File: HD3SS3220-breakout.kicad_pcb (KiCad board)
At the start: 4 copper layers, 74.1 x 58 mm, 30 parts, among them J2 USB_C_Receptacle, SW2 SW_DIP_x04, U4 HD3SS3220RNHR, U5 U-A-39SS-Y-1, U6 HT7533-1_C14289, U7 TPD4EUSB30, U8 TPD2EUSB30, U9 PZ254-2-08-WS

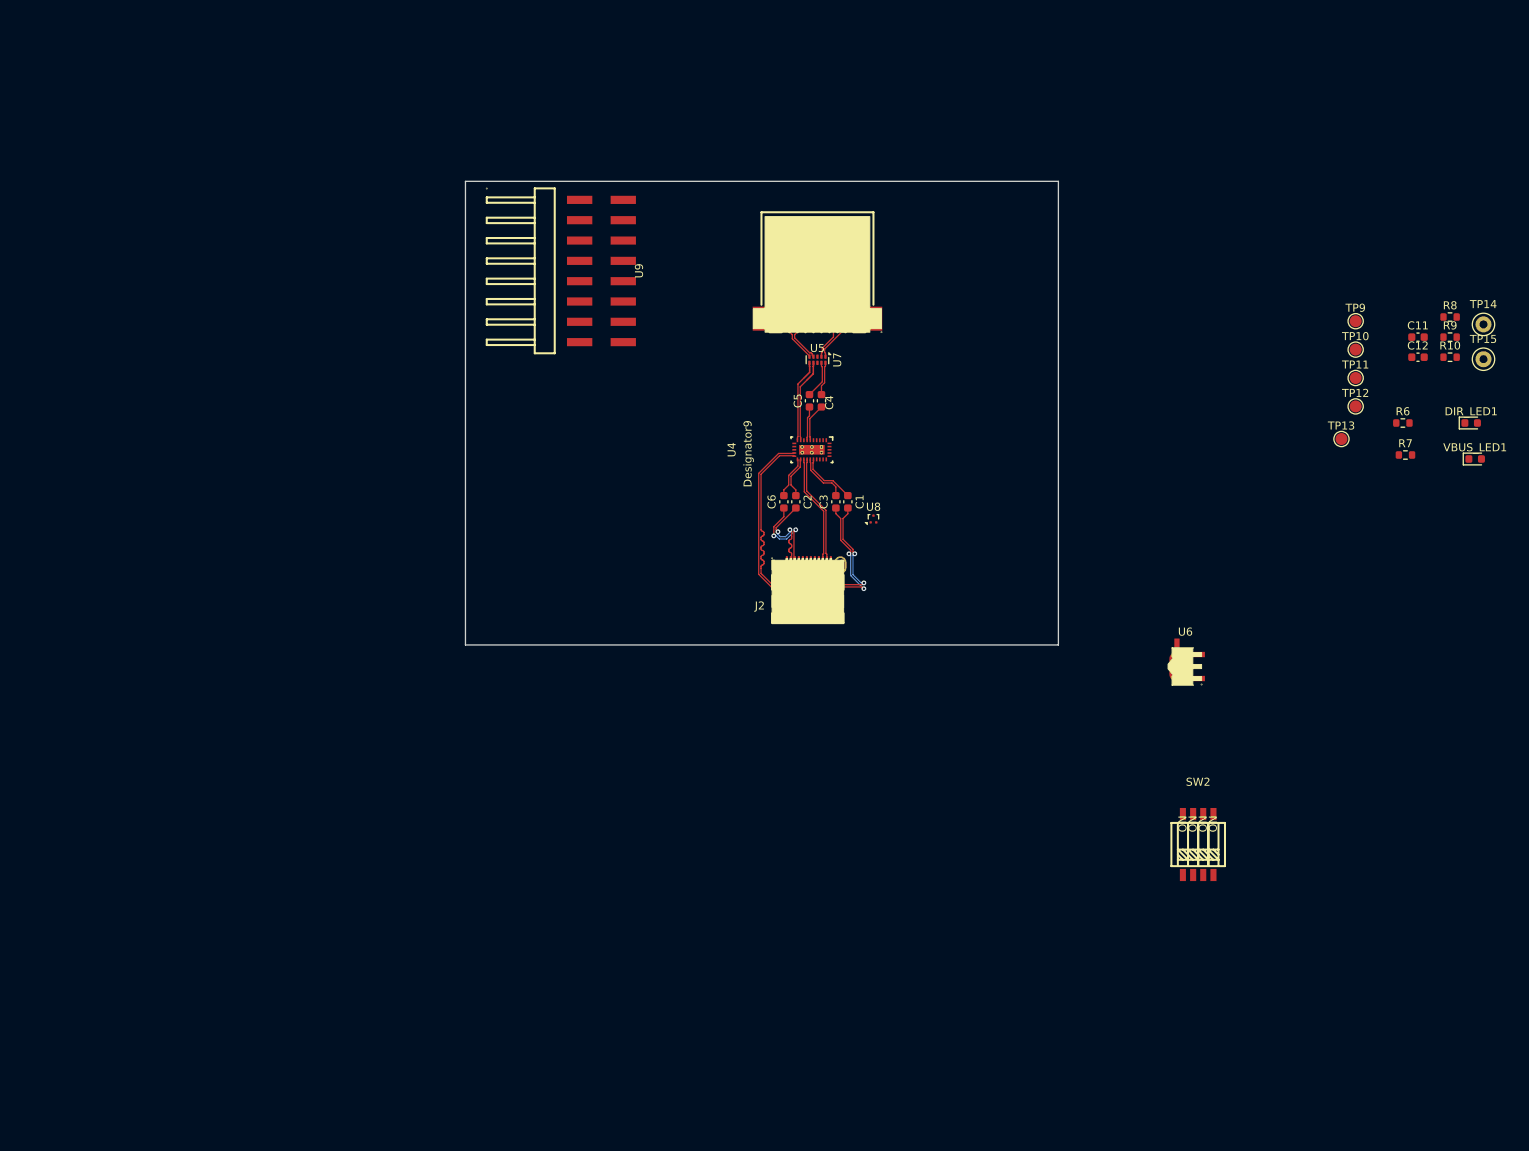
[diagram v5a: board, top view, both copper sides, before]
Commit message: Routing Complete (DRC Checker Errors needs fixing)
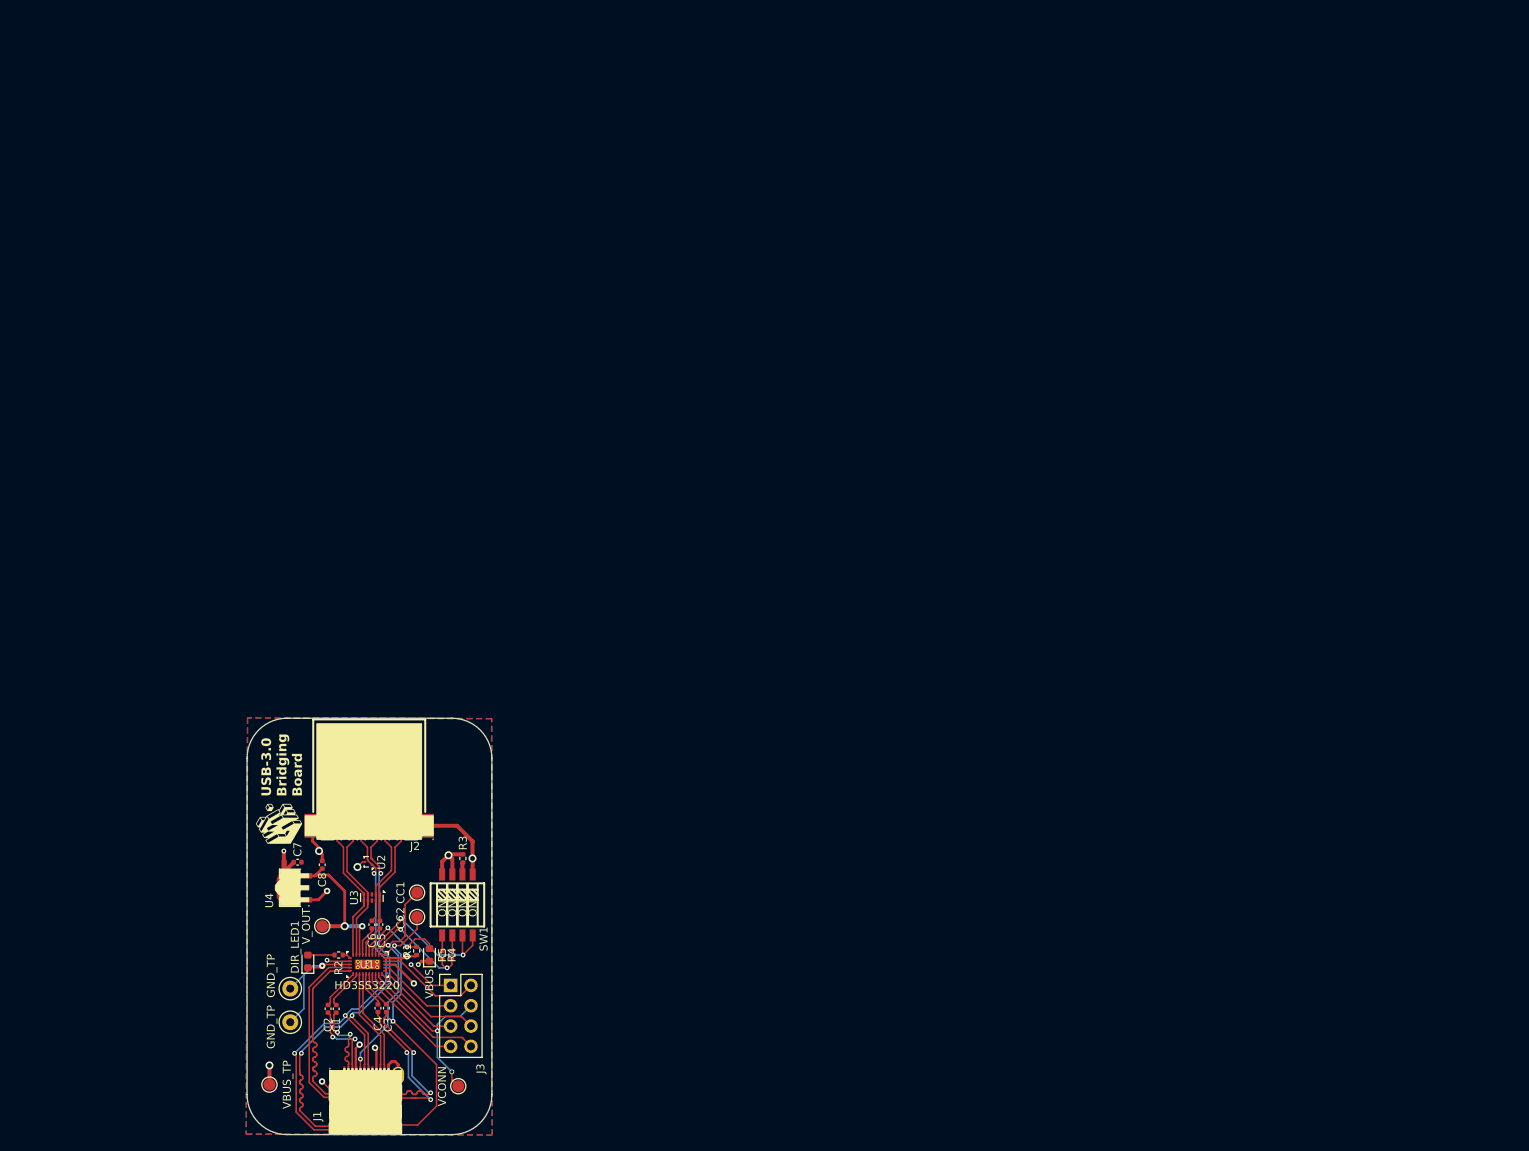
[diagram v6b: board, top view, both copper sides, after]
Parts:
- removed C11, C12: 10uF, Capacitor_SMD:C_0603_1608Metric
- removed R10: 200K, Resistor_SMD:R_0603_1608Metric
- removed R6: 1K, Resistor_SMD:R_0603_1608Metric
- removed R7: 500K, Resistor_SMD:R_0603_1608Metric
- removed R8: 10K, Resistor_SMD:R_0603_1608Metric
- removed R9: 900K, Resistor_SMD:R_0603_1608Metric
- removed SW2: SW_DIP_x04, Button_Switch_SMD:SW4
- removed TP10: CC2, TestPoint:TestPoint_Pad_D1.5mm
- removed TP11: VBUS, TestPoint:TestPoint_Pad_D1.5mm
- removed TP12: VCC33, TestPoint:TestPoint_Pad_D1.5mm
- removed TP13: VCONN, TestPoint:TestPoint_Pad_D1.5mm
- removed TP14: GND1, TestPoint:TestPoint_Keystone_5000-5004_Miniature
- removed TP15: GND2, TestPoint:TestPoint_Keystone_5000-5004_Miniature
- removed TP9: CC1, TestPoint:TestPoint_Pad_D1.5mm
- removed U5: U-A-39SS-Y-1, footprint:USB-3.0-A_U-A-39SS-Y-1
- removed U6: HT7533-1_C14289, footprint:SOT-89-3_L4.5-W2.5-P1.50-LS4.2-BR
- removed U7: TPD4EUSB30, Package_SON:USON-10_2.5x1.0mm_P0.5mm
- removed U8: TPD2EUSB30, Package_TO_SOT_SMD:Texas_DRT-3
- removed U9: PZ254-2-08-WS, footprint:HDR-SMD_16P-P2.54-H-M-R2-C8-W12.0-N
- removed VBUS_LED1: LED, LED_SMD:LED_0603_1608Metric
- added C7: 10uF, Capacitor_SMD:C_0402_1005Metric, F.Cu at (121.5, 105.4)
- added C8: 10uF, Capacitor_SMD:C_0402_1005Metric, F.Cu at (124.6, 105.7)
- added CC1: CC1, TestPoint:TestPoint_Pad_D1.5mm, F.Cu at (136.4, 109.2)
- added CC2: CC2, TestPoint:TestPoint_Pad_D1.5mm, F.Cu at (136.4, 112.2)
- added G***: LOGO, LOGO, F.Cu at (119.2, 100.6)
- added GND_TP: GND1, TestPoint:TestPoint_Keystone_5000-5004_Miniature, F.Cu at (120.6, 125.4)
- added GND_TP: GND2, TestPoint:TestPoint_Keystone_5000-5004_Miniature, F.Cu at (120.6, 121.2)
- added J1: USB_C_Receptacle, Interface_USB:USB-C-SMD_TYPE-C-USB-19, F.Cu at (130.0, 134.0)
- added J3: A2541WV-2x4P, Connector_PinHeader_2.54mm:PinHeader_2x04_P2.54mm_Vertical, F.Cu at (140.7, 120.8)
- added R1: 900K, Resistor_SMD:R_0402_1005Metric, F.Cu at (136.4, 116.5)
- added R2: 200K, Resistor_SMD:R_0402_1005Metric, F.Cu at (126.7, 117.0)
- added R3: 1K, Resistor_SMD:R_0402_1005Metric, F.Cu at (142.2, 104.9)
- added R4: 500K, Resistor_SMD:R_0402_1005Metric, F.Cu at (140.8, 117.0)
- added R5: 10K, Resistor_SMD:R_0402_1005Metric, F.Cu at (139.6, 117.0)
- added SW1: SW_DIP_x04, Button_Switch_SMD:SW4, F.Cu at (141.5, 110.7)
- added U1: HD3SS3220RNHR, Interface_USB:HD3SS3220IRNHR, F.Cu at (130.3, 118.2)
- added U2: TPD2EUSB30, Package_TO_SOT_SMD:Texas_DRT-3, F.Cu at (130.4, 105.3)
- added U3: TPD4EUSB30, Package_SON:USON-10_2.5x1.0mm_P0.5mm, F.Cu at (130.8, 109.8)
- added VBUS: LED, LED_SMD:LED_0603_1608Metric, F.Cu at (138.0, 117.0)
- added VBUS_TP: VBUS, TestPoint:TestPoint_Pad_D1.5mm, F.Cu at (118.0, 133.2)
- added VCONN: VCONN, TestPoint:TestPoint_Pad_D1.5mm, F.Cu at (141.6, 133.4)
- added V_OUT: VCC33, TestPoint:TestPoint_Pad_D1.5mm, F.Cu at (124.6, 113.4)
- C1, C2, C3, C4, C5, C6: footprint Capacitor_SMD:C_0603_1608Metric -> Capacitor_SMD:C_0402_1005Metric
- J2: value USB_C_Receptacle -> U-A-39SS-Y-1; footprint to-be-organized:USB-C-SMD_TYPE-C-USB-19 -> Interface_USB:USB-3.0-A_U-A-39SS-Y-1
- U4: value HD3SS3220RNHR -> HT7533-1_C14289; footprint Interface_USB:HD3SS3220IRNHR -> Interface_USB:SOT-89-3_L4.5-W2.5-P1.50-LS4.2-BR
- moved DIR_LED1 160.2 mm to (122.8, 117.8), turned to 90 degrees
- moved C4 94.0 mm to (131.6, 123.6)
- moved C1 90.0 mm to (126.3, 123.7)
- moved C2 86.2 mm to (125.3, 123.7), turned to 90 degrees
- moved U4 84.7 mm to (121.2, 108.6), turned to 0 degrees
- moved C5 84.7 mm to (131.8, 113.2)
- moved C3 84.6 mm to (132.6, 123.6)
- moved C6 73.8 mm to (130.8, 113.2), turned to 90 degrees
- moved J2 63.0 mm to (130.5, 101.2), turned to 180 degrees
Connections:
- C1 pad 1: /TX2+ -> /Type-C Interface & High-Speed Mux/TX1+
- C1 pad 2: /TX2+ -> /Type-C Interface & High-Speed Mux/TX1_IC+
- C2 pad 1: /TX1+ -> /Type-C Interface & High-Speed Mux/TX1-
- C2 pad 2: /TX1+ -> /Type-C Interface & High-Speed Mux/TX1_IC-
- C3 pad 1: /TX2- -> /Type-C Interface & High-Speed Mux/TX2+
- C3 pad 2: /TX2- -> /Type-C Interface & High-Speed Mux/TX2_IC+
- C4 pad 1: /SSTXMUX+ -> /Type-C Interface & High-Speed Mux/TX2-
- C4 pad 2: /SSTX+ -> /Type-C Interface & High-Speed Mux/TX2_IC-
- C5 pad 1: /SSTXMUX- -> /Type-C Interface & High-Speed Mux/SSTXMUX+
- C5 pad 2: /SSTX- -> /Type-A Interface/SSTX+
- C6 pad 1: /TX1- -> /Type-C Interface & High-Speed Mux/SSTXMUX-
- C6 pad 2: /TX1- -> /Type-A Interface/SSTX-
- U4 pad 1: /CC2 -> GND
- U4 pad 2: /CC1 -> VBUS
- U4 pad 3: /MODE -> /Power Management, Configuration & Debug/V_OUT
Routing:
- net /Type-A Interface/D+: track 0.00 -> 64.5 mm, vias 0 -> 3
- net /Type-A Interface/D-: track 0.00 -> 64.2 mm, vias 0 -> 3
- net GND: track 0.00 -> 59.2 mm, vias 0 -> 10
- net /Type-C Interface & High-Speed Mux/CC2: track 0.00 -> 43.4 mm, vias 0 -> 2
- net VBUS: track 0.00 -> 39.5 mm, vias 0 -> 9
- net /Type-C Interface & High-Speed Mux/CC1: track 0.00 -> 28.7 mm, vias 0 -> 2
- net /Type-C Interface & High-Speed Mux/RX1-: track 0.00 -> 25.8 mm
- net /Type-C Interface & High-Speed Mux/RX1+: track 0.00 -> 25.7 mm
- net /TX2-: track 25.0 -> 0.00 mm, vias 2 -> 0
- net /RX1-: track 24.9 -> 0.00 mm
- net /RX1+: track 24.7 -> 0.00 mm
- net /Power Management, Configuration & Debug/VCONN: track 0.00 -> 24.5 mm, vias 0 -> 2
- net /TX2+: track 24.4 -> 0.00 mm, vias 2 -> 0
- net /Type-C Interface & High-Speed Mux/TX2-: track 0.00 -> 22.0 mm, vias 0 -> 2
- net /Type-C Interface & High-Speed Mux/TX2+: track 0.00 -> 21.9 mm, vias 0 -> 2
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- added copper zone on B.Cu, net GND
- added copper zone on F.Cu, net GND
- added copper zone on In1.Cu, net GND
- added copper zone on In2.Cu, net VBUS
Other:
- board size 74.1 x 58 mm -> 30.6 x 52 mm
- board text added: "USB-3.0 Bridging Board"

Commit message: DRC Errors Fixed, BOM Cleaned up and Generated, Gerber Generated
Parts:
- R1, R4: footprint Resistor_SMD:R_0402_1005Metric -> Resistor_SMD:R_0805_2012Metric
- moved R4 18.0 mm to (154.5, 105.3), turned to 0 degrees
- moved C7 17.7 mm to (137.8, 98.3), turned to -90 degrees
- moved R1 17.6 mm to (148.4, 103.6)
- moved R5 17.5 mm to (151.8, 104.4)
- moved VBUS_LED1 17.5 mm to (150.2, 104.3)
- moved C4 17.3 mm to (143.3, 111.0)
- moved C8 17.3 mm to (136.4, 93.1)
- moved CC1 17.3 mm to (148.2, 96.6)
- moved CC2 17.3 mm to (148.2, 99.6)
- moved GND_TP 17.3 mm to (132.4, 112.8)
- moved VCONN_TP 17.3 mm to (153.4, 120.8)
- moved C1 17.3 mm to (138.1, 111.1)
- moved C2 17.3 mm to (137.1, 111.1)
- moved C3 17.3 mm to (144.4, 111.0)
- moved C5 17.3 mm to (143.6, 100.6)
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- renumbered V_OUT to TP3, VBUS to VBUS_LED1, VCONN to VCONN_TP
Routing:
- net GND: track 59.2 -> 68.0 mm
- net /Power Management, Configuration & Debug/PORT: track 21.2 -> 25.9 mm
- net /Power Management, Configuration & Debug/MODE: track 15.4 -> 18.4 mm
- net Net-(DIR_LED1-A): track 2.84 -> 5.75 mm
- net Net-(U1-VBUS_DET): track 13.0 -> 15.0 mm
- net /Power Management, Configuration & Debug/V_OUT: track 20.1 -> 22.0 mm
- net Net-(R4-Pad1): track 1.96 -> 3.75 mm
- net VBUS: track 39.5 -> 38.4 mm
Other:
- board text added: "2026"

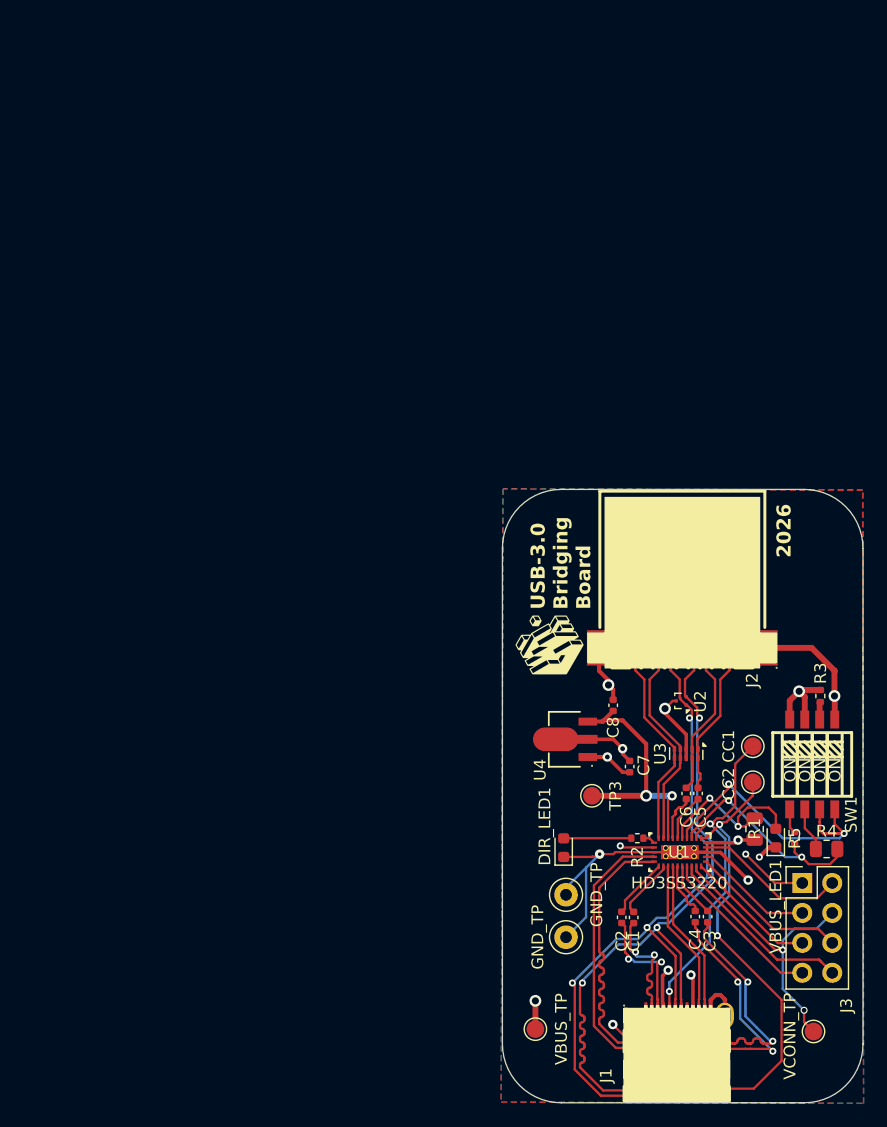
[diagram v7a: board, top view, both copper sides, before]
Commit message: Hopefully final DRC error fixed by reducing Minimum Spoke Count from 2 to 1
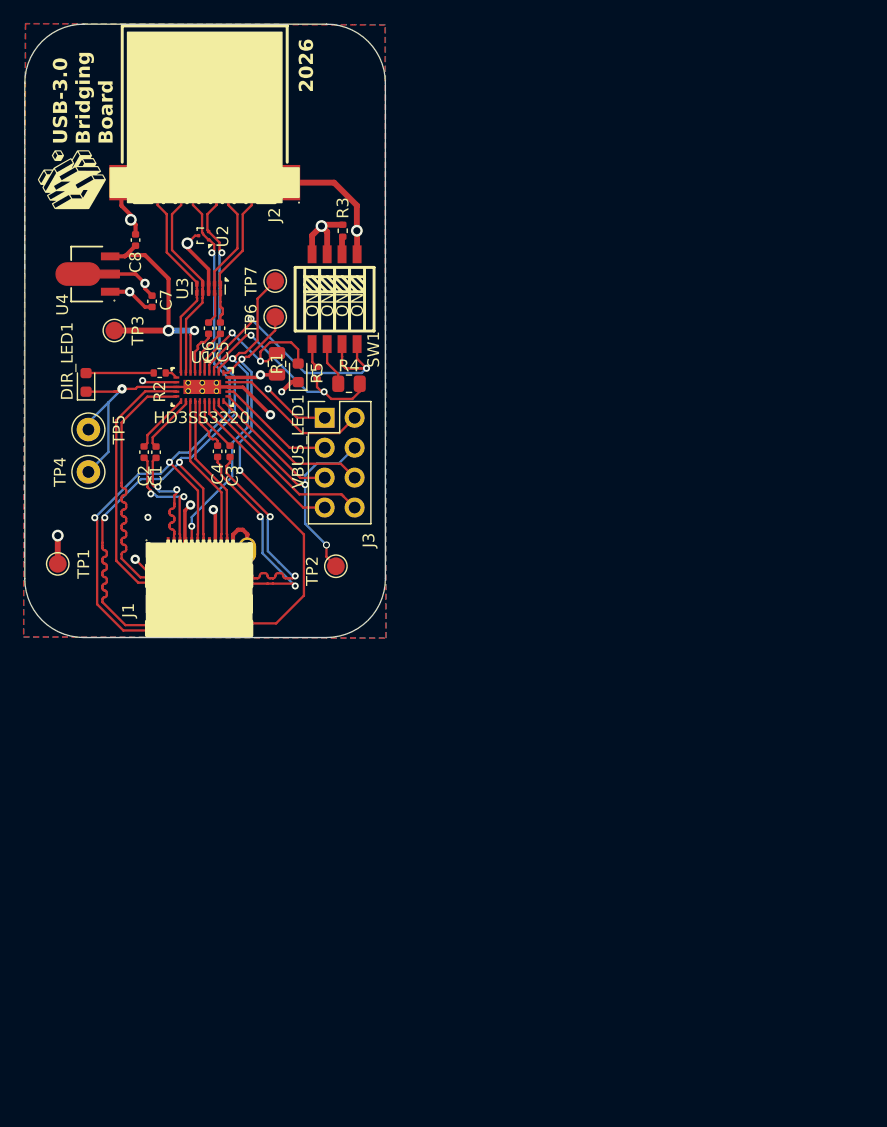
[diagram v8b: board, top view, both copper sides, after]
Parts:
- moved R1 56.6 mm to (107.8, 64.1)
- moved TP2 56.6 mm to (112.8, 81.3)
- moved TP4 56.6 mm to (91.8, 73.3)
- moved C8 56.6 mm to (95.8, 53.6)
- moved G*** 56.6 mm to (90.4, 48.5)
- moved J2 56.6 mm to (101.7, 49.1)
- moved SW1 56.6 mm to (112.7, 58.6)
- moved TP5 56.6 mm to (91.8, 69.7)
- moved C1 56.6 mm to (97.6, 71.6)
- moved C3 56.6 mm to (103.8, 71.5)
- moved C4 56.6 mm to (102.8, 71.5)
- moved C5 56.6 mm to (103.0, 61.1)
- moved C6 56.6 mm to (102.0, 61.1)
- moved R3 56.6 mm to (113.4, 52.8)
- moved R4 56.6 mm to (113.9, 65.8)
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- renumbered VBUS_TP to TP1, VCONN_TP to TP2, GND_TP to TP4, GND_TP to TP5, CC2 to TP6, CC1 to TP7
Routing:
- net GND: vias 10 -> 11
